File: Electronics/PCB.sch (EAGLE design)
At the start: 9 parts, among them IC1 7805T

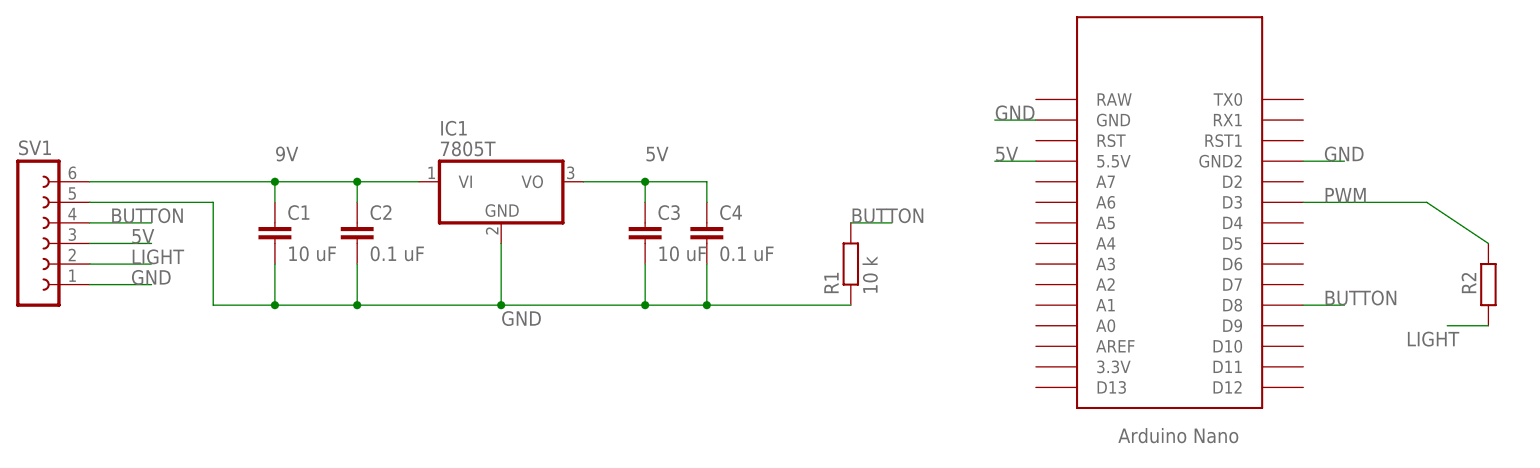
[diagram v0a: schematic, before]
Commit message: removed regulator, changed some pins for better routing
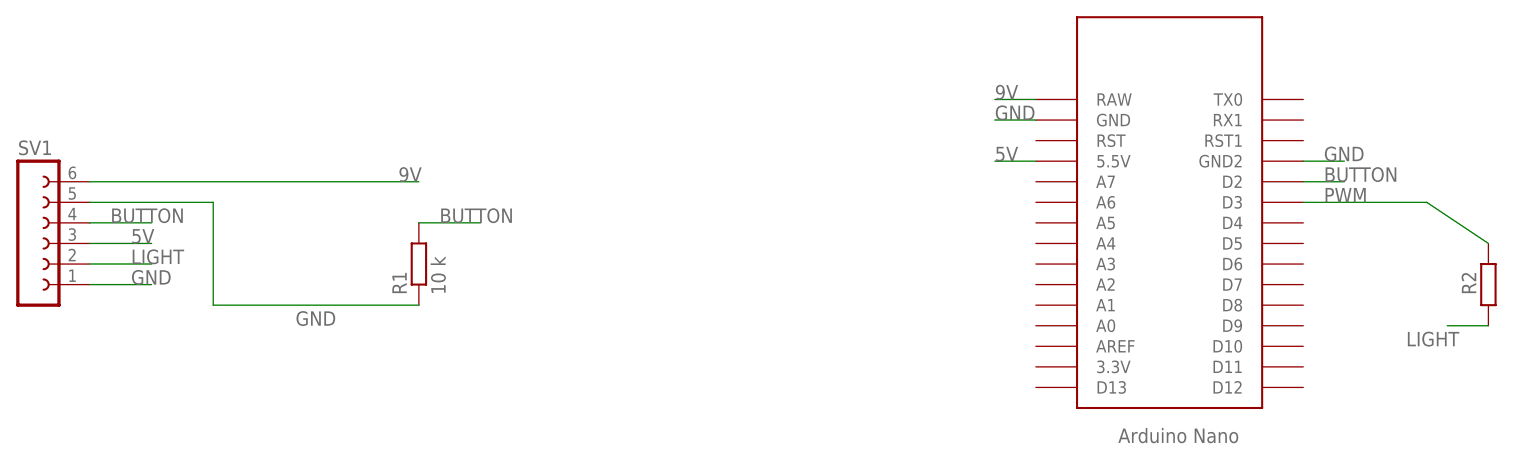
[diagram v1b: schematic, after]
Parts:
- removed C1, C3: 10 uF, eagle-ltspice:C
- removed C2, C4: 0.1 uF, eagle-ltspice:C
- removed IC1: 7805T, adafruit:7805T
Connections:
- net 5V: no longer C3.1, C4.1, IC1.VO
- net 9V: now also U$1.RAW; no longer C1.1, C2.1, IC1.VI
- net BUTTON: now also U$1.D2; no longer U$1.D8
- net GND: no longer C1.2, C2.2, C3.2, C4.2, IC1.GND
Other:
- moved on the sheet: R1
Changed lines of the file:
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@@
 </classes>
 <parts>
-<part name="C1" library="eagle-ltspice" library_urn="urn:adsk.eagle:library:217" deviceset="C" device="" package3d_urn="urn:adsk.eagle:package:13265/1" value="10 uF"/>
-<part name="C2" library="eagle-ltspice" library_urn="urn:adsk.eagle:library:217" deviceset="C" device="" package3d_urn="urn:adsk.eagle:package:13265/1" value="0.1 uF"/>
-<part name="C3" library="eagle-ltspice" library_urn="urn:adsk.eagle:library:217" deviceset="C" device="" package3d_urn="urn:adsk.eagle:package:13265/1" value="10 uF"/>
-<part name="C4" library="eagle-ltspice" library_urn="urn:adsk.eagle:library:217" deviceset="C" device="" package3d_urn="urn:adsk.eagle:package:13265/1" value="0.1 uF"/>
 <part name="R1" library="eagle-ltspice" library_urn="urn:adsk.eagle:library:217" deviceset="R" device="" package3d_urn="urn:adsk.eagle:package:13300/1" value="10 k"/>
 <part name="R2" library="eagle-ltspice" library_urn="urn:adsk.eagle:library:217" deviceset="R" device="" package3d_urn="urn:adsk.eagle:package:13300/1"/>
 <part name="SV1" library="con-lsta" library_urn="urn:adsk.eagle:library:161" deviceset="FE06-1" device="" package3d_urn="urn:adsk.eagle:package:8191/1"/>
 <part name="U$1" library="Arduino-clone" deviceset="NANO" device=""/>
-<part name="IC1" library="adafruit" library_urn="urn:adsk.eagle:library:420" deviceset="78*" device="T" package3d_urn="urn:adsk.eagle:package:6240670/1" technology="05"/>
 </parts>
 <sheets>
@@
 </plain>
 <instances>
-<instance part="C1" gate="G$1" x="22.86" y="81.28">
-<attribute name="NAME" x="24.384" y="81.661" size="1.778" layer="95"/>
-<attribute name="VALUE" x="24.384" y="76.581" size="1.778" layer="96"/>
-</instance>
-<instance part="C2" gate="G$1" x="33.02" y="81.28">
-<attribute name="NAME" x="34.544" y="81.661" size="1.778" layer="95"/>
-<attribute name="VALUE" x="34.544" y="76.581" size="1.778" layer="96"/>
-</instance>
-<instance part="C3" gate="G$1" x="68.58" y="81.28">
-<attribute name="NAME" x="70.104" y="81.661" size="1.778" layer="95"/>
-<attribute name="VALUE" x="70.104" y="76.581" size="1.778" layer="96"/>
-</instance>
-<instance part="C4" gate="G$1" x="76.2" y="81.28">
-<attribute name="NAME" x="77.724" y="81.661" size="1.778" layer="95"/>
-<attribute name="VALUE" x="77.724" y="76.581" size="1.778" layer="96"/>
-</instance>
-<instance part="R1" gate="G$1" x="93.98" y="76.2" rot="R90">
-<attribute name="NAME" x="92.4814" y="72.39" size="1.778" layer="95" rot="R90"/>
-<attribute name="VALUE" x="97.282" y="72.39" size="1.778" layer="96" rot="R90"/>
+<instance part="R1" gate="G$1" x="40.64" y="76.2" rot="R90">
+<attribute name="NAME" x="39.1414" y="72.39" size="1.778" layer="95" rot="R90"/>
+<attribute name="VALUE" x="43.942" y="72.39" size="1.778" layer="96" rot="R90"/>
 </instance>
 <instance part="R2" gate="G$1" x="172.72" y="73.66" rot="R90">
@@
 </instance>
 <instance part="U$1" gate="G$1" x="139.7" y="76.2" rot="MR180"/>
-<instance part="IC1" gate="A1" x="50.8" y="86.36">
-<attribute name="NAME" x="43.18" y="92.075" size="1.778" layer="95"/>
-<attribute name="VALUE" x="43.18" y="89.535" size="1.778" layer="96"/>
-</instance>
 </instances>
 <busses>
@@
 <segment>
 <pinref part="SV1" gate="G$1" pin="6"/>
-<pinref part="C1" gate="G$1" pin="1"/>
-<wire x1="0" y1="86.36" x2="22.86" y2="86.36" width="0.1524" layer="91"/>
-<wire x1="22.86" y1="86.36" x2="22.86" y2="83.82" width="0.1524" layer="91"/>
-<pinref part="C2" gate="G$1" pin="1"/>
-<wire x1="33.02" y1="83.82" x2="33.02" y2="86.36" width="0.1524" layer="91"/>
-<wire x1="33.02" y1="86.36" x2="22.86" y2="86.36" width="0.1524" layer="91"/>
-<junction x="22.86" y="86.36"/>
-<pinref part="IC1" gate="A1" pin="VI"/>
-<wire x1="40.64" y1="86.36" x2="33.02" y2="86.36" width="0.1524" layer="91"/>
-<junction x="33.02" y="86.36"/>
-<label x="22.86" y="88.9" size="1.778" layer="95"/>
+<wire x1="0" y1="86.36" x2="40.64" y2="86.36" width="0.1524" layer="91"/>
+<label x="38.1" y="86.36" size="1.778" layer="95"/>
+</segment>
+<segment>
+<pinref part="U$1" gate="G$1" pin="RAW"/>
+<wire x1="116.84" y1="96.52" x2="111.76" y2="96.52" width="0.1524" layer="91"/>
+<label x="111.76" y="96.52" size="1.778" layer="95"/>
 </segment>
 </net>
@@
 <wire x1="0" y1="83.82" x2="15.24" y2="83.82" width="0.1524" layer="91"/>
 <wire x1="15.24" y1="83.82" x2="15.24" y2="71.12" width="0.1524" layer="91"/>
-<wire x1="15.24" y1="71.12" x2="22.86" y2="71.12" width="0.1524" layer="91"/>
-<pinref part="C1" gate="G$1" pin="2"/>
-<wire x1="22.86" y1="71.12" x2="22.86" y2="76.2" width="0.1524" layer="91"/>
-<pinref part="C2" gate="G$1" pin="2"/>
-<wire x1="33.02" y1="76.2" x2="33.02" y2="71.12" width="0.1524" layer="91"/>
-<wire x1="33.02" y1="71.12" x2="22.86" y2="71.12" width="0.1524" layer="91"/>
-<junction x="22.86" y="71.12"/>
-<pinref part="IC1" gate="A1" pin="GND"/>
-<wire x1="50.8" y1="78.74" x2="50.8" y2="71.12" width="0.1524" layer="91"/>
-<wire x1="50.8" y1="71.12" x2="33.02" y2="71.12" width="0.1524" layer="91"/>
-<junction x="33.02" y="71.12"/>
-<label x="50.8" y="68.58" size="1.778" layer="95"/>
-<pinref part="C3" gate="G$1" pin="2"/>
-<wire x1="68.58" y1="76.2" x2="68.58" y2="71.12" width="0.1524" layer="91"/>
-<wire x1="68.58" y1="71.12" x2="50.8" y2="71.12" width="0.1524" layer="91"/>
-<junction x="50.8" y="71.12"/>
-<pinref part="C4" gate="G$1" pin="2"/>
-<wire x1="76.2" y1="76.2" x2="76.2" y2="71.12" width="0.1524" layer="91"/>
-<wire x1="76.2" y1="71.12" x2="68.58" y2="71.12" width="0.1524" layer="91"/>
-<junction x="68.58" y="71.12"/>
+<label x="25.4" y="68.58" size="1.778" layer="95"/>
+<wire x1="40.64" y1="71.12" x2="15.24" y2="71.12" width="0.1524" layer="91"/>
 <pinref part="R1" gate="G$1" pin="1"/>
-<wire x1="93.98" y1="71.12" x2="76.2" y2="71.12" width="0.1524" layer="91"/>
-<junction x="76.2" y="71.12"/>
 </segment>
 <segment>
@@
 <net name="5V" class="0">
 <segment>
-<pinref part="IC1" gate="A1" pin="VO"/>
-<wire x1="60.96" y1="86.36" x2="68.58" y2="86.36" width="0.1524" layer="91"/>
-<pinref part="C3" gate="G$1" pin="1"/>
-<wire x1="68.58" y1="86.36" x2="68.58" y2="83.82" width="0.1524" layer="91"/>
-<pinref part="C4" gate="G$1" pin="1"/>
-<wire x1="76.2" y1="83.82" x2="76.2" y2="86.36" width="0.1524" layer="91"/>
-<wire x1="76.2" y1="86.36" x2="68.58" y2="86.36" width="0.1524" layer="91"/>
-<junction x="68.58" y="86.36"/>
-<label x="68.58" y="88.9" size="1.778" layer="95"/>
-</segment>
-<segment>
 <pinref part="U$1" gate="G$1" pin="5.5V"/>
 <wire x1="116.84" y1="88.9" x2="111.76" y2="88.9" width="0.1524" layer="91"/>
@@
 <segment>
 <pinref part="R1" gate="G$1" pin="2"/>
-<wire x1="93.98" y1="81.28" x2="99.06" y2="81.28" width="0.1524" layer="91"/>
-<label x="93.98" y="81.28" size="1.778" layer="95"/>
+<wire x1="40.64" y1="81.28" x2="48.26" y2="81.28" width="0.1524" layer="91"/>
+<label x="43.18" y="81.28" size="1.778" layer="95"/>
 </segment>
 <segment>
@@
 </segment>
 <segment>
-<pinref part="U$1" gate="G$1" pin="D8"/>
-<wire x1="149.86" y1="71.12" x2="154.94" y2="71.12" width="0.1524" layer="91"/>
-<label x="152.4" y="71.12" size="1.778" layer="95"/>
+<pinref part="U$1" gate="G$1" pin="D2"/>
+<wire x1="149.86" y1="86.36" x2="154.94" y2="86.36" width="0.1524" layer="91"/>
+<label x="152.4" y="86.36" size="1.778" layer="95"/>
 </segment>
 </net>

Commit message: Final PCB Design
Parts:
- R2: value (none) -> 220
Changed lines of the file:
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@@
 <parts>
 <part name="R1" library="eagle-ltspice" library_urn="urn:adsk.eagle:library:217" deviceset="R" device="" package3d_urn="urn:adsk.eagle:package:13300/1" value="10 k"/>
-<part name="R2" library="eagle-ltspice" library_urn="urn:adsk.eagle:library:217" deviceset="R" device="" package3d_urn="urn:adsk.eagle:package:13300/1"/>
+<part name="R2" library="eagle-ltspice" library_urn="urn:adsk.eagle:library:217" deviceset="R" device="" package3d_urn="urn:adsk.eagle:package:13300/1" value="220"/>
 <part name="SV1" library="con-lsta" library_urn="urn:adsk.eagle:library:161" deviceset="FE06-1" device="" package3d_urn="urn:adsk.eagle:package:8191/1"/>
 <part name="U$1" library="Arduino-clone" deviceset="NANO" device=""/>
